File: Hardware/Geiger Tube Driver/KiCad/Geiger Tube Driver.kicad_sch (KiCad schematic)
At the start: 40 parts, among them J1 I/O, Q1 MMBT3904, Q2 STN2580, Q3 MMBT3904, Q4 MMBT3906, U1 NE555D

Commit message: Geiger Tube Driver Rev 1.1
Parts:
- H1, H2, H3, H4: footprint MountingHole:MountingHole_3.2mm_M3_Pad -> Footprints:MountingHole_3.2mm_M3_Pad_Via
- R16: value 330 -> 1k
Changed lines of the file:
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@@
   (title_block
     (title "Geiger Tube Driver")
-    (date "2023-09-21")
-    (rev "1.0")
+    (date "2023-12-29")
+    (rev "1.1")
     (company "https://github.com/median-dispersion/SBM-20-Geiger-Counter")
   )
@@
       (effects (font (size 1.27 1.27)) (justify left))
     )
-    (property "Footprint" "MountingHole:MountingHole_3.2mm_M3_Pad" (at 22.225 180.975 0)
+    (property "Footprint" "Footprints:MountingHole_3.2mm_M3_Pad_Via" (at 22.225 180.975 0)
       (effects (font (size 1.27 1.27)) hide)
     )
@@
       (effects (font (size 1.27 1.27)) (justify left))
     )
-    (property "Footprint" "MountingHole:MountingHole_3.2mm_M3_Pad" (at 22.225 173.99 0)
+    (property "Footprint" "Footprints:MountingHole_3.2mm_M3_Pad_Via" (at 22.225 173.99 0)
       (effects (font (size 1.27 1.27)) hide)
     )
@@
       (effects (font (size 1.27 1.27)) (justify left))
     )
-    (property "Value" "330" (at 246.38 116.205 0)
+    (property "Value" "1k" (at 246.38 116.205 0)
       (effects (font (size 1.27 1.27)) (justify left))
     )
@@
       (effects (font (size 1.27 1.27)) (justify left))
     )
-    (property "Footprint" "MountingHole:MountingHole_3.2mm_M3_Pad" (at 22.225 187.96 0)
+    (property "Footprint" "Footprints:MountingHole_3.2mm_M3_Pad_Via" (at 22.225 187.96 0)
       (effects (font (size 1.27 1.27)) hide)
     )
@@
       (effects (font (size 1.27 1.27)) (justify left))
     )
-    (property "Footprint" "MountingHole:MountingHole_3.2mm_M3_Pad" (at 22.225 194.31 0)
-      (effects (font (size 1.27 1.27)) hide)
-    )
+    (property "Footprint" "Footprints:MountingHole_3.2mm_M3_Pad_Via" (at 22.225 194.31 0)
+      (effects (font (size 1.27 1.27)) hide)
+    )

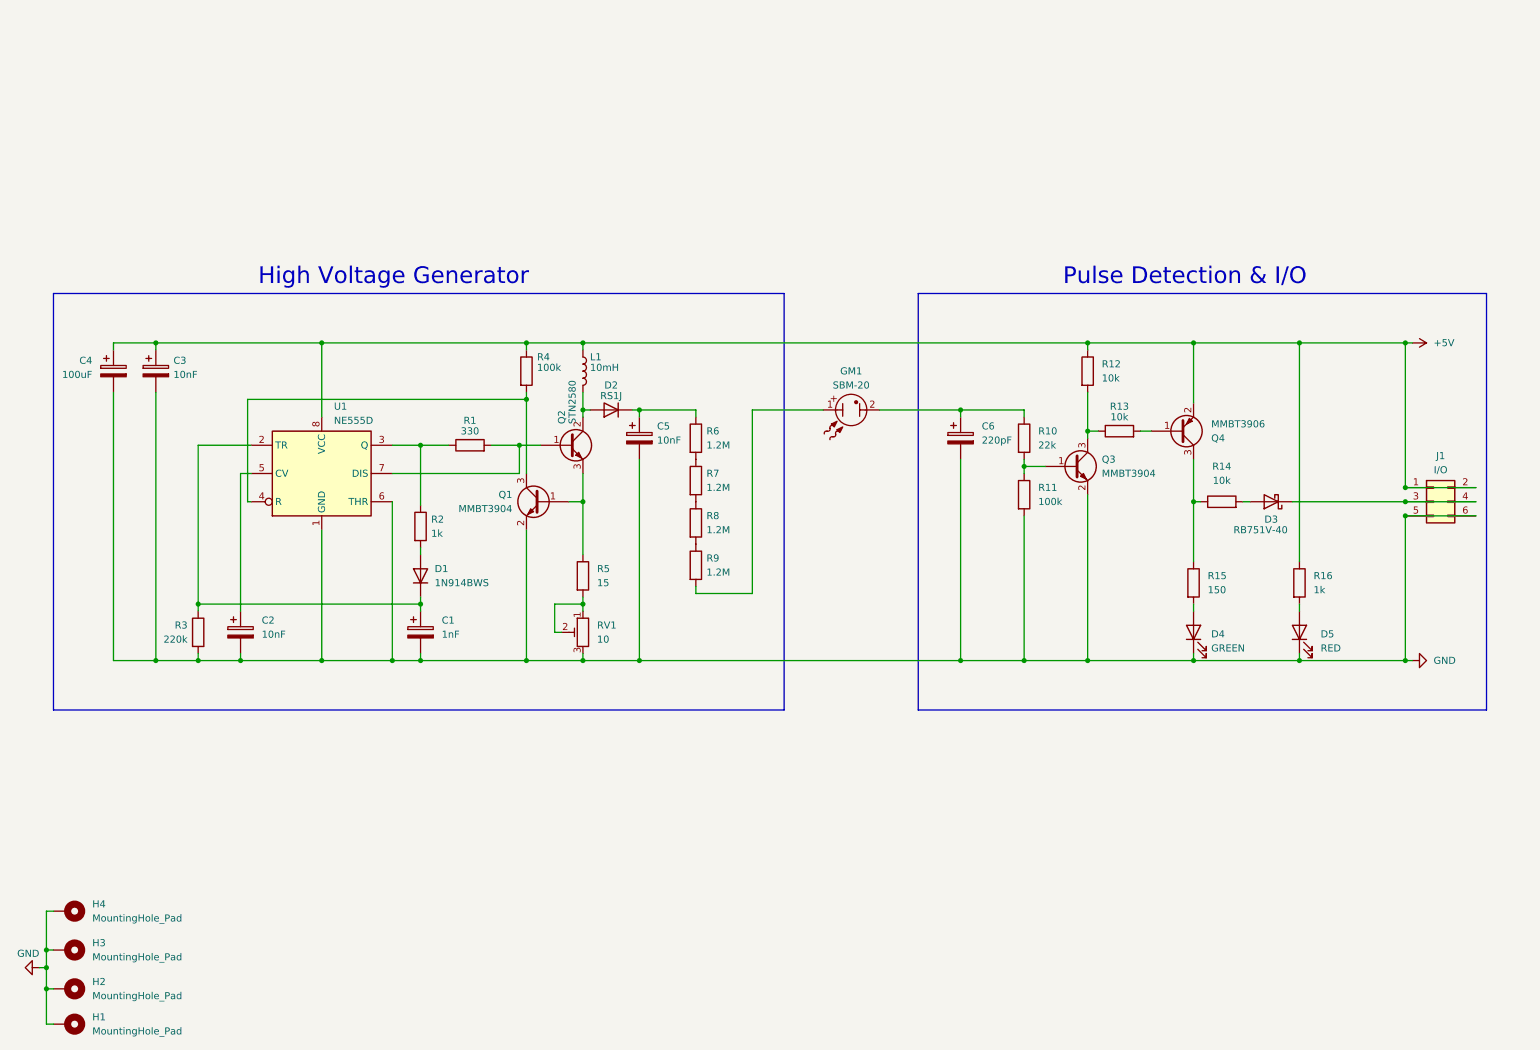
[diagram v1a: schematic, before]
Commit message: Organized schematics & rounded PCB corners
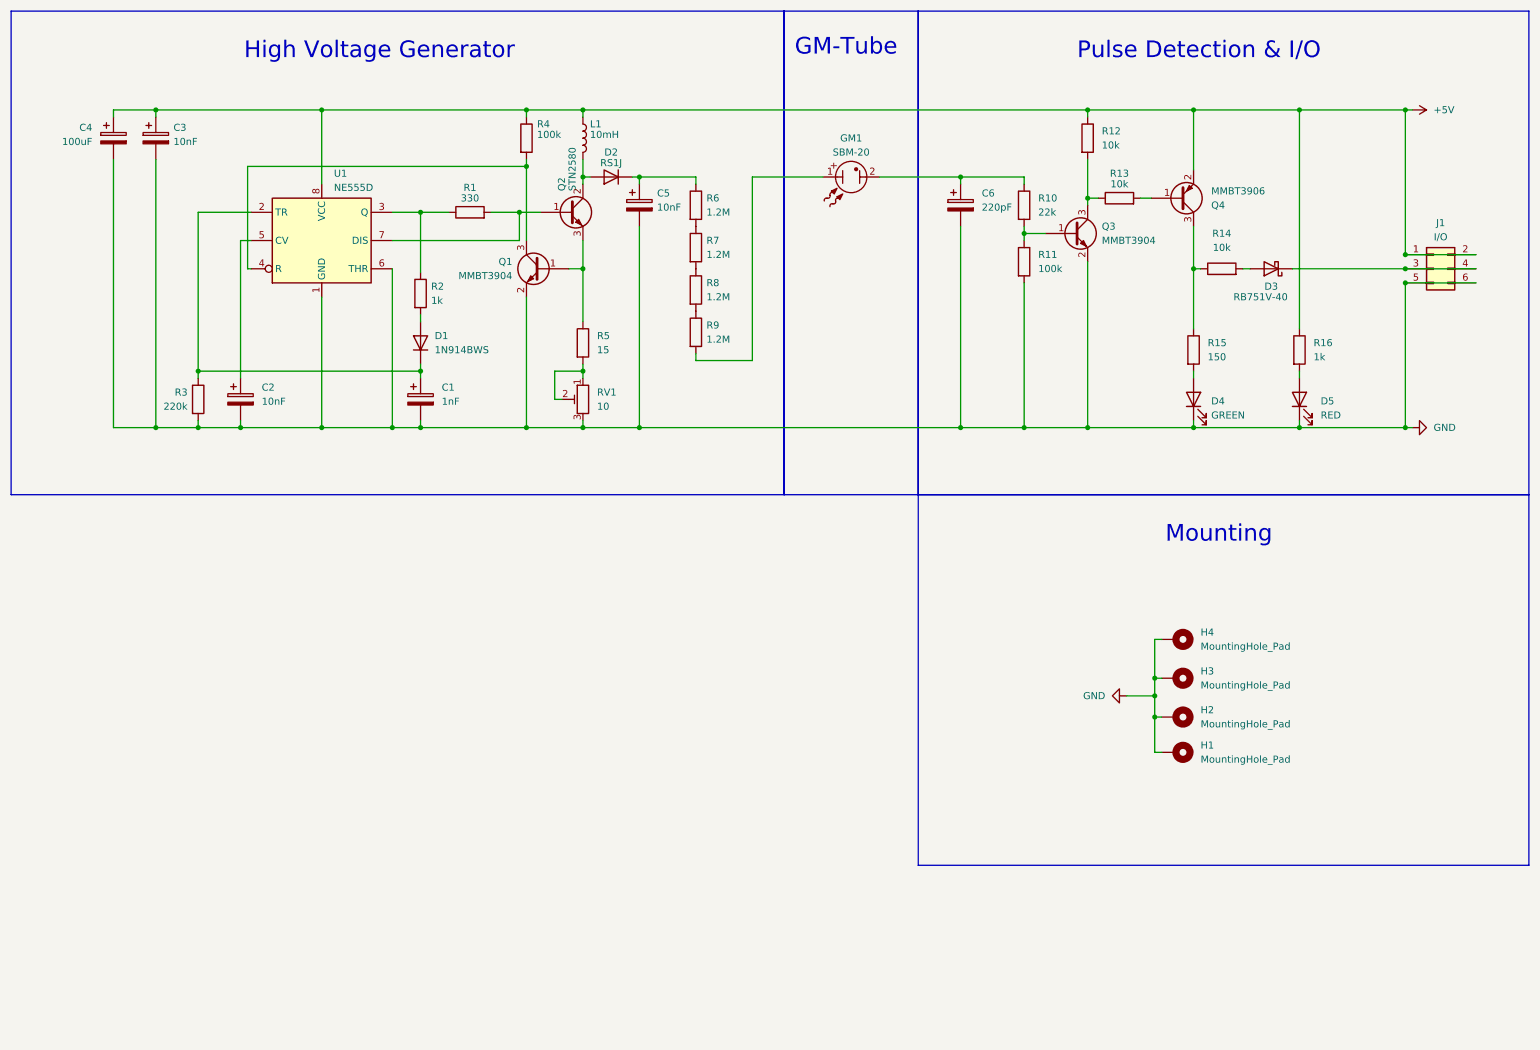
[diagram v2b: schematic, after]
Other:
- note added: "GM-Tube"
- note added: "Mounting"
- moved on the sheet: C1, C2, C3, C4, C5, C6, D1, D2, D3, D4, D5, GM1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
